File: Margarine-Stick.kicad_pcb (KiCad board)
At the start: 2 copper layers, 226.1 x 40.6 mm, 42 parts

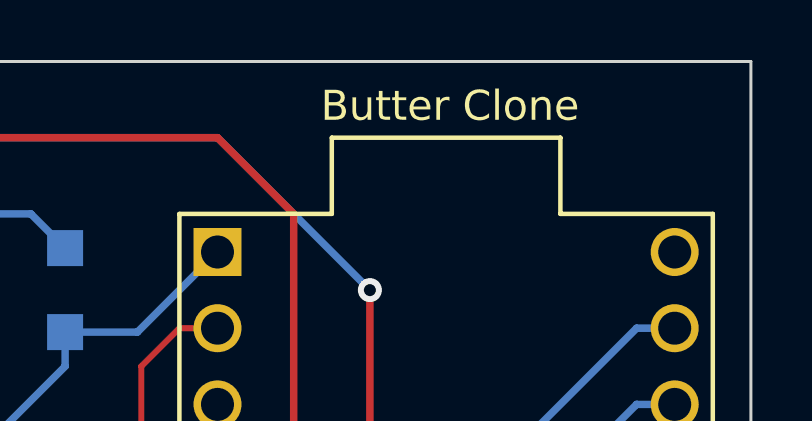
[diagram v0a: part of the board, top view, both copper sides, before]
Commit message: feat: correct silkscreen
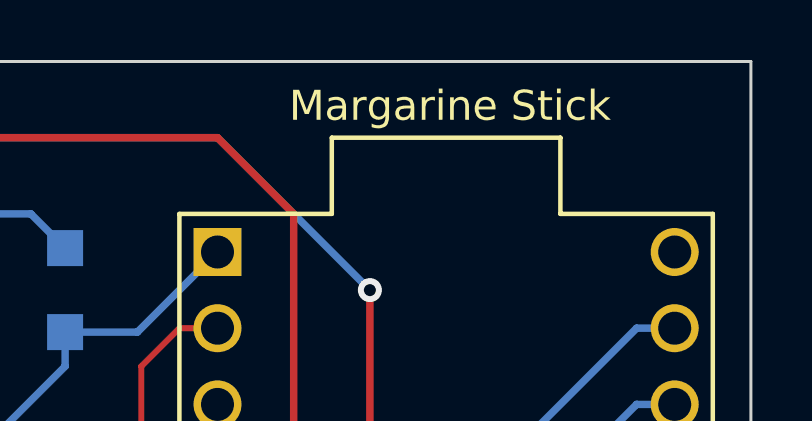
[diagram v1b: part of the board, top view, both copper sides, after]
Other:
- board text added: "Margarine Stick"
- board text removed: "Butter Clone"
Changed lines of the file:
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@@
   (gr_line (start 251.46 30.48) (end 251.46 71.12) (layer "Edge.Cuts") (width 0.1))
   (gr_line (start 25.4 71.12) (end 25.4 30.48) (layer "Edge.Cuts") (width 0.1))
-  (gr_text "Butter Clone" (at 241.43 31.96) (layer "F.SilkS")
+  (gr_text "Margarine Stick" (at 241.43 31.96) (layer "F.SilkS")
     (effects (font (size 1 1) (thickness 0.15)))
   )
